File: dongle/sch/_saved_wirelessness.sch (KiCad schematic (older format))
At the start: 16 parts, among them IC1 ATMEGA8A-P, J1 DB9, P1 NRF24L01, SW10 SW_PUSH, SW9 SW_PUSH, U1 NCP1117ST33T3G, X1 12M

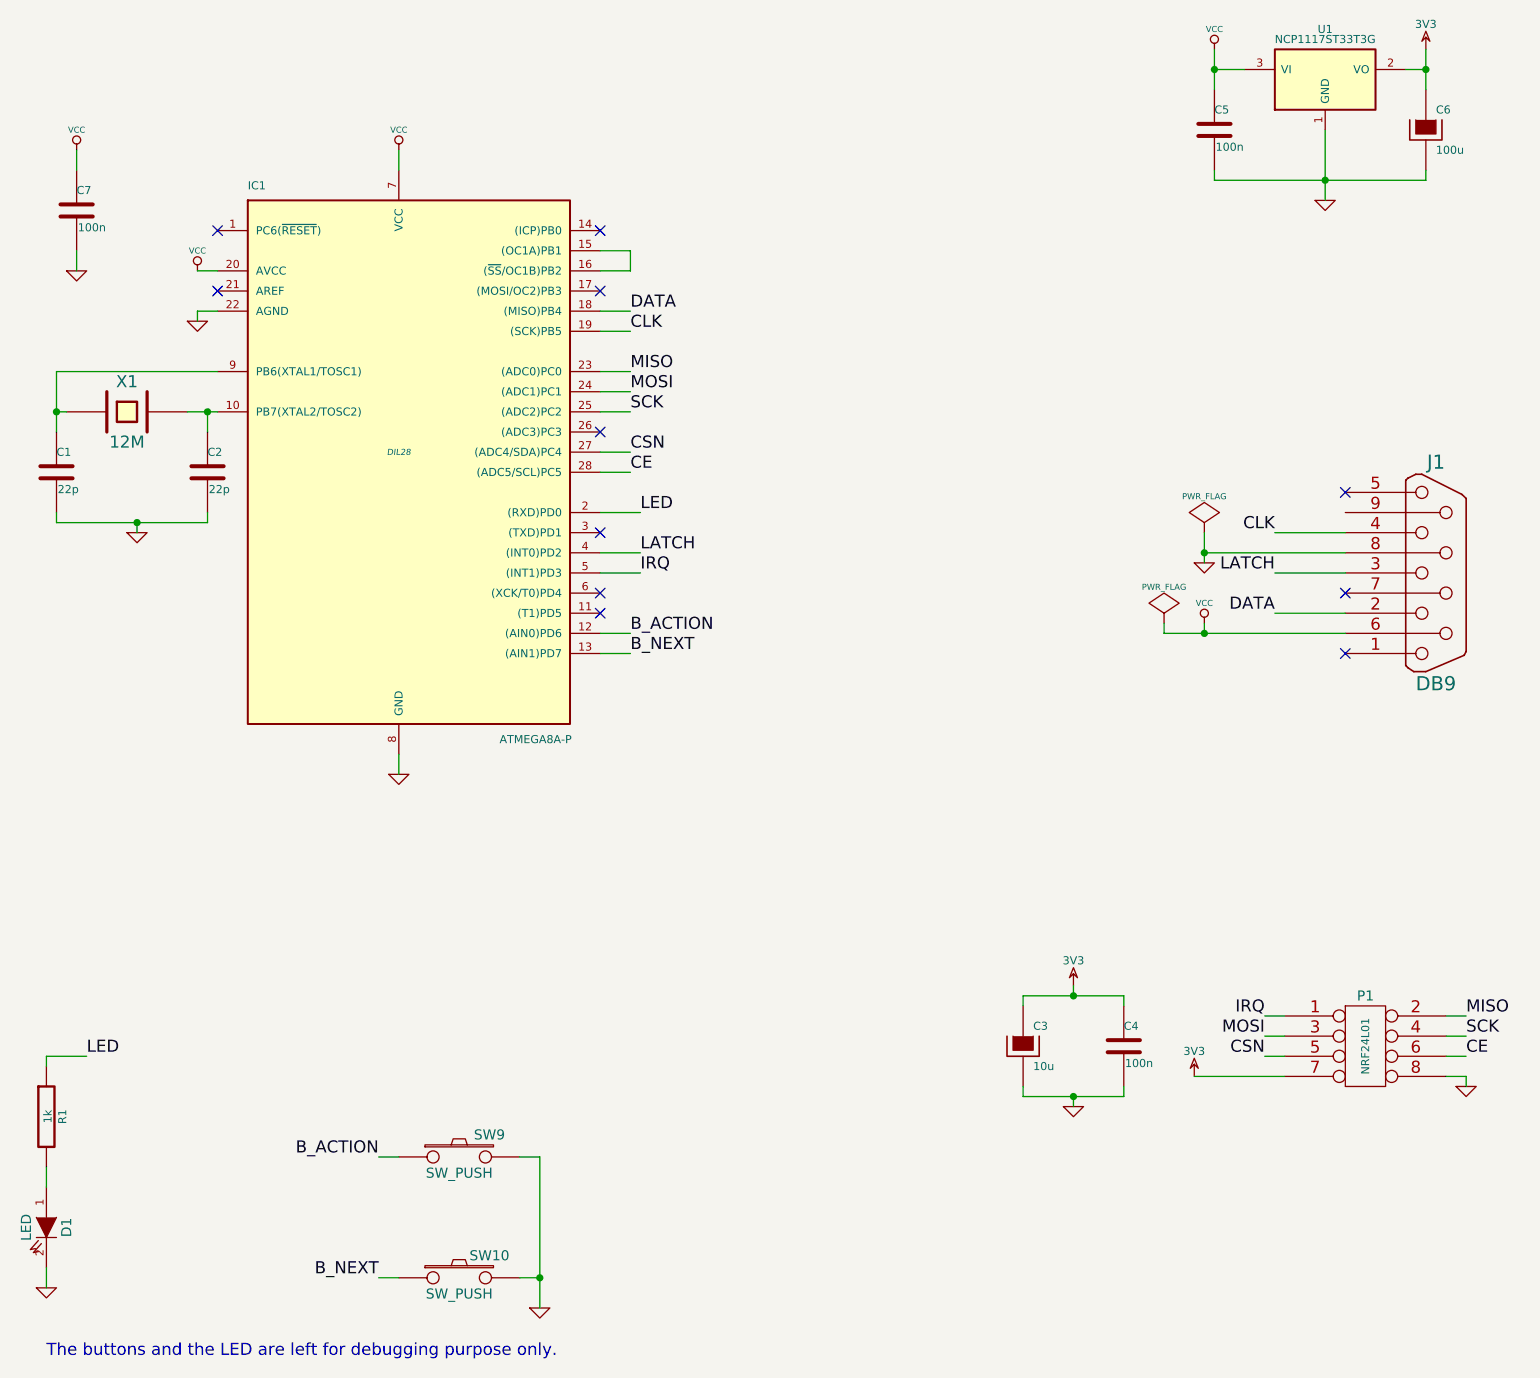
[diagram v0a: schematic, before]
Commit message: clean-up, schematics and source code for the dongle are now consistent
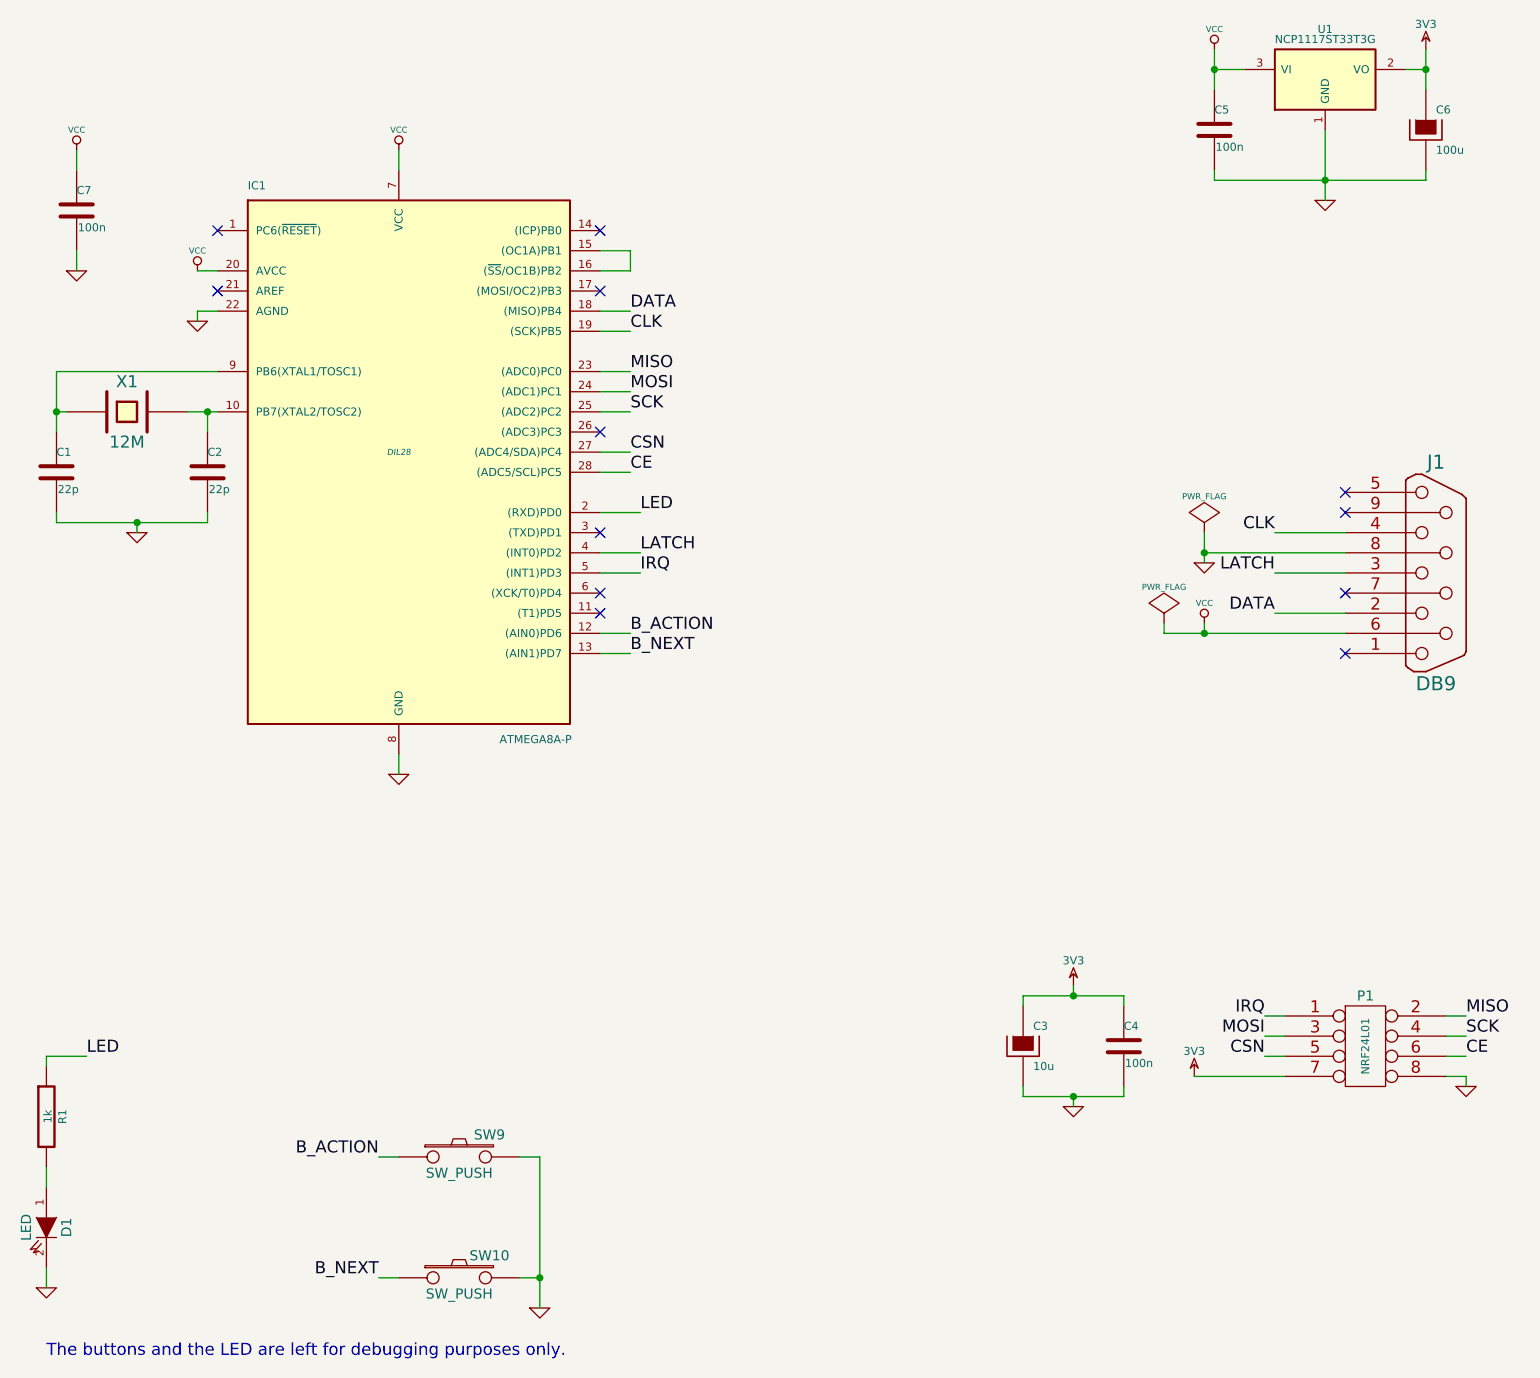
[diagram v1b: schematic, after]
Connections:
- no-connect marks 11 -> 12
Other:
- note added: "The buttons and the LED are left for debugging purposes only."
- note removed: "The buttons and the LED are left for debugging purpose only."
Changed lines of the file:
@@
 NoConn ~ 6500 2800
 Text Notes 3750 7400 0    60   ~ 0
-The buttons and the LED are left for debugging purpose only.
+The buttons and the LED are left for debugging purposes only.
 $Comp
 L R R1
@@
 	9500 3750 9500 3800
 Connection ~ 9500 3800
+NoConn ~ 10200 3200
 $EndSCHEMATC
